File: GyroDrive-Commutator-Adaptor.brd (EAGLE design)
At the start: 108 x 76.2 mm, 26 parts, among them U1 HALL, U2 PCA9517, U3 5V, U4 2.5V, U5 INA2141U, U6 INA2141U, U7 INA2141U, X1 NORCOMP-DB25-SMD-MALE

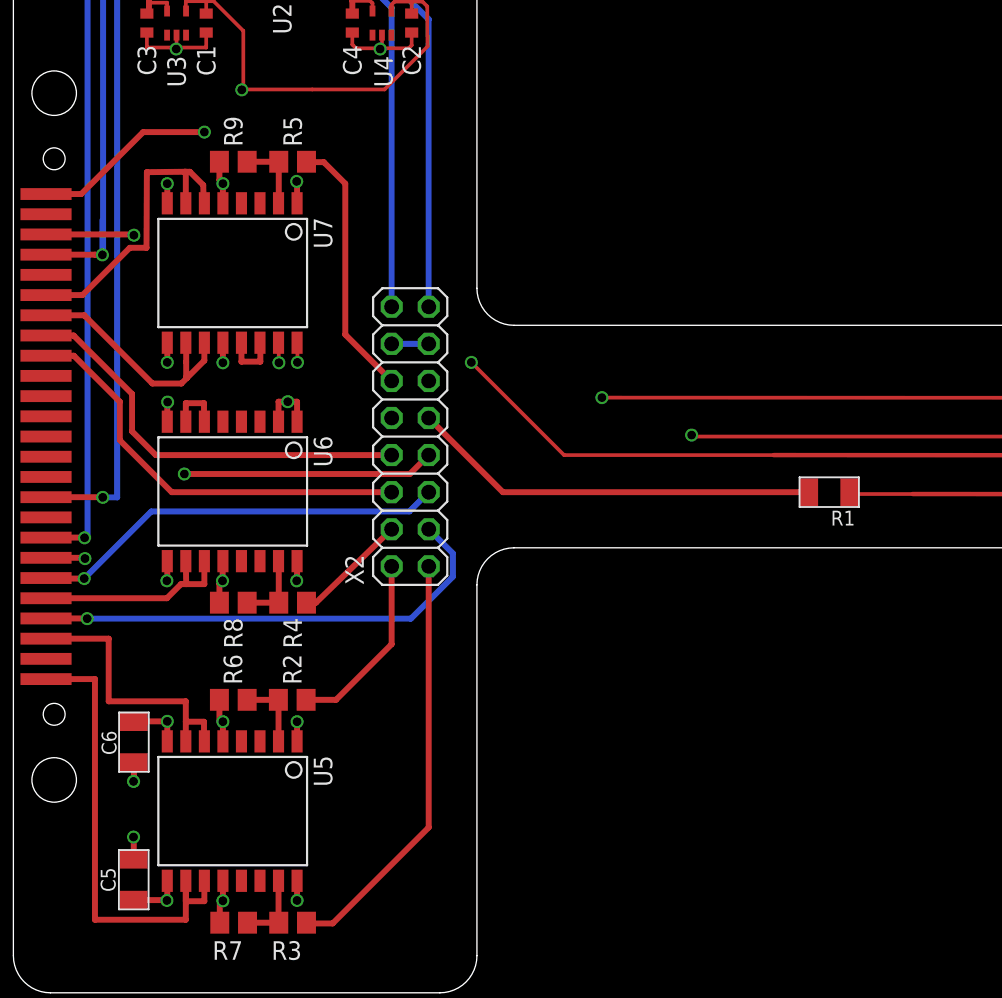
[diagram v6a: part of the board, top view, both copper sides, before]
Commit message: Fixed stop mask DRC errors on some resistors and capacitors
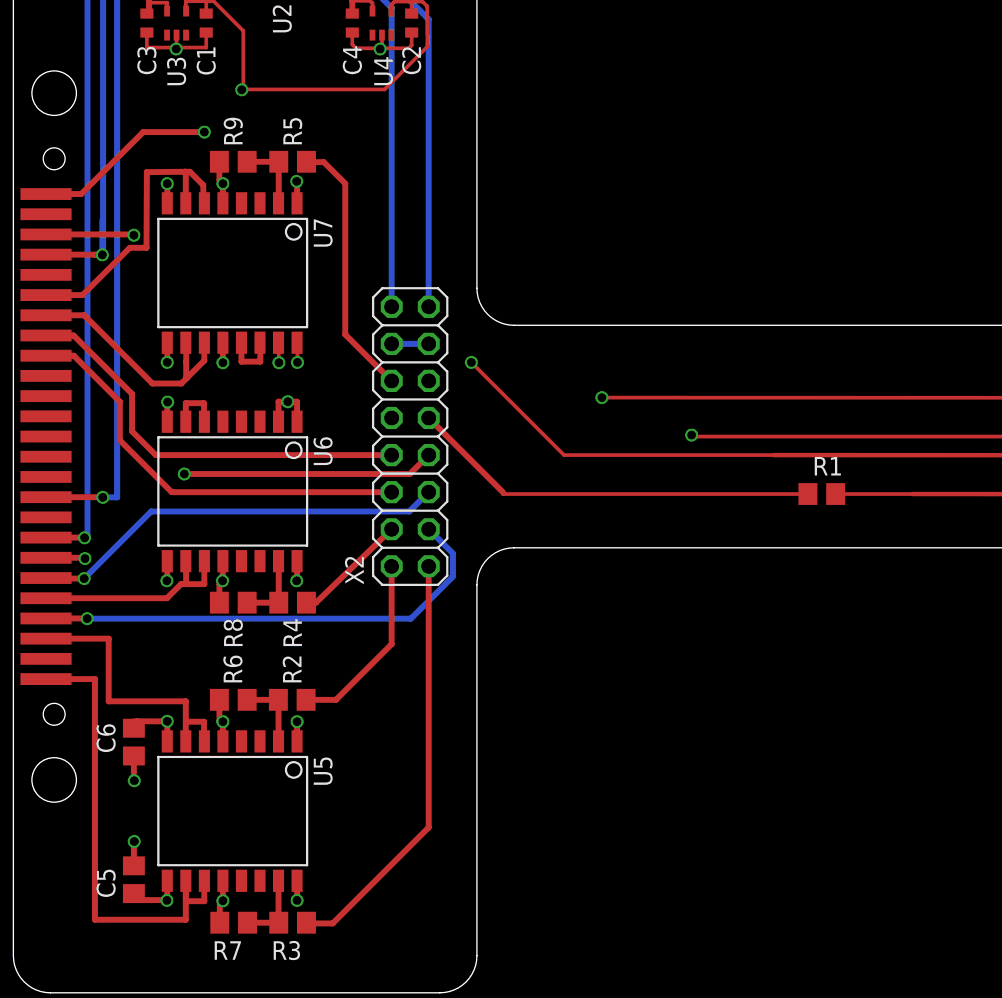
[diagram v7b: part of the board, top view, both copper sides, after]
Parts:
- C5, C6: device elm:R0805ELM -> resistor:C0805
- R1: device elm:R0805ELM -> resistor:R0805
- moved R1 0.52 mm to (55.4, 34.2), turned to 0 degrees
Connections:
- net V+: now also R1.1; no longer R1.2
- net V+_HALL: now also R1.2; no longer R1.1
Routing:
- net AGND: track 97.8 -> 99.9 mm
- net V-: track 73.9 -> 75.3 mm
- net V+_HALL: track 48.5 -> 49.4 mm
- net V+: track 185.1 -> 185.7 mm
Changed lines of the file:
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@@
 <attribute name="OC_FARNELL" value="1459468" x="-30.734" y="40.6908" size="1.778" layer="27" rot="R180" display="off"/>
-</element>
-<element name="R1" library="elm" package="R0805ELM" value="10k" x="55.88" y="34.29" rot="R180"/>
-<element name="C5" library="elm" package="R0805ELM" value="100nF" x="8.244471875" y="7.746809375" smashed="yes" rot="R90">
-<attribute name="NAME" x="6.999871875" y="7.746809375" size="1.016" layer="25" ratio="15" rot="R90" align="bottom-center"/>
-<attribute name="VALUE" x="8.244471875" y="7.772209375" size="1.016" layer="27" ratio="15" align="center"/>
-</element>
-<element name="C6" library="elm" package="R0805ELM" value="100nF" x="8.255" y="17.1704" smashed="yes" rot="R270">
-<attribute name="NAME" x="6.0452" y="17.9578" size="1.016" layer="25" ratio="15" rot="R270"/>
-<attribute name="VALUE" x="8.255" y="17.145" size="1.016" layer="27" ratio="15" rot="R180" align="center"/>
 </element>
 <element name="X2" library="pinhead" package="2X08" value="" x="27.178" y="38.1" rot="R90"/>
@@
 <attribute name="VALUE" x="10.7442" y="70.3072" size="1.27" layer="27" rot="R270"/>
 </element>
+<element name="R1" library="resistor" package="R0805" value="10k" x="55.372" y="34.163"/>
+<element name="C5" library="resistor" package="C0805" value="100nF" x="8.255" y="7.747" rot="R90"/>
+<element name="C6" library="resistor" package="C0805" value="100nF" x="8.255" y="17.1704" smashed="yes" rot="R270">
+<attribute name="NAME" x="5.715" y="18.4912" size="1.27" layer="25" rot="R270"/>
+<attribute name="VALUE" x="5.715" y="18.4404" size="1.27" layer="27" rot="R270"/>
+</element>
 </elements>
 <signals>
 <signal name="V-">
-<contactref element="C6" pad="1"/>
 <contactref element="U6" pad="8"/>
 <contactref element="U7" pad="8"/>
@@
 <wire x1="10.541" y1="18.5928" x2="10.5156" y2="18.542" width="0.4064" layer="2"/>
 <wire x1="10.5156" y1="18.542" x2="10.1346" y2="18.542" width="0.4064" layer="2"/>
-<wire x1="8.255" y1="18.5674" x2="8.255" y2="18.5928" width="0.4064" layer="1"/>
-<wire x1="8.255" y1="18.5928" x2="10.541" y2="18.5928" width="0.4064" layer="1"/>
+<wire x1="8.255" y1="18.5928" x2="8.4836" y2="18.5928" width="0.4064" layer="1"/>
+<wire x1="8.4836" y1="18.5928" x2="10.541" y2="18.5928" width="0.4064" layer="1"/>
 <wire x1="10.541" y1="39.116" x2="10.541" y2="40.4114" width="0.4064" layer="1"/>
 <wire x1="10.541" y1="40.4114" x2="10.5664" y2="40.4622" width="0.4064" layer="1"/>
@@
 <wire x1="11.7094" y1="35.5346" x2="9.45374375" y2="35.5346" width="0.4064" layer="2"/>
 <wire x1="9.45374375" y1="35.5346" x2="9.40294375" y2="35.4838" width="0.4064" layer="2"/>
+<contactref element="C6" pad="1"/>
+<wire x1="8.255" y1="18.1204" x2="8.1788" y2="18.1204" width="0.254" layer="1"/>
+<wire x1="8.1788" y1="18.1204" x2="8.1788" y2="17.8308" width="0.254" layer="1"/>
+<wire x1="8.1788" y1="17.8308" x2="8.4836" y2="17.8308" width="0.254" layer="1"/>
+<wire x1="8.4836" y1="17.8308" x2="8.4836" y2="18.5928" width="0.254" layer="1"/>
 </signal>
 <signal name="V+">
 <contactref element="U5" pad="9"/>
 <contactref element="U6" pad="9"/>
-<contactref element="R1" pad="2"/>
-<contactref element="C5" pad="1"/>
 <contactref element="U7" pad="9"/>
 <contactref element="X1" pad="P$1"/>
@@
 <via x="10.5156" y="6.3246" extent="1-16" drill="0.6"/>
 <wire x1="10.4902" y1="6.35" x2="10.5156" y2="6.3246" width="0.4064" layer="1"/>
-<wire x1="10.4902" y1="6.35" x2="8.2446625" y2="6.35" width="0.4064" layer="1"/>
-<wire x1="8.2446625" y1="6.35" x2="8.244471875" y2="6.349809375" width="0.4064" layer="1"/>
+<wire x1="10.4902" y1="6.35" x2="8.3566" y2="6.35" width="0.4064" layer="1"/>
 <via x="10.5156" y="28.2194" extent="1-16" drill="0.6"/>
+<wire x1="8.3566" y1="6.35" x2="8.2446625" y2="6.35" width="0.4064" layer="1"/>
 <wire x1="10.541" y1="44.5262" x2="10.541" y2="43.18" width="0.4064" layer="1"/>
 <via x="10.541" y="43.18" extent="1-16" drill="0.6"/>
@@
 <wire x1="15.6972" y1="61.8998" x2="15.6464" y2="61.849" width="0.4064" layer="2"/>
 <via x="15.6464" y="61.849" extent="1-16" drill="0.6"/>
-<wire x1="20.4724" y1="61.8744" x2="15.6718" y2="61.8744" width="0.254" layer="1"/>
 <wire x1="15.6718" y1="61.8744" x2="15.6464" y2="61.849" width="0.4064" layer="1"/>
 <wire x1="12.3698" y1="58.9534" x2="13.081" y2="58.9534" width="0.4064" layer="2"/>
-<wire x1="54.483" y1="34.29" x2="33.528" y2="34.29" width="0.4064" layer="1"/>
 <wire x1="33.528" y1="34.29" x2="28.448" y2="39.37" width="0.4064" layer="1"/>
 <wire x1="28.448" y1="39.37" x2="27.2034" y2="38.1254" width="0.4064" layer="2"/>
@@
 <wire x1="26.1112" y1="67.8942" x2="27.2796" y2="67.8942" width="0.254" layer="1"/>
 <wire x1="27.2796" y1="67.8942" x2="27.2796" y2="67.071" width="0.254" layer="1"/>
-<wire x1="20.4724" y1="61.8744" x2="25.4254" y2="61.8744" width="0.254" layer="1"/>
+<wire x1="15.6718" y1="61.8744" x2="25.4254" y2="61.8744" width="0.254" layer="1"/>
 <wire x1="25.4254" y1="61.8744" x2="28.3718" y2="64.8208" width="0.254" layer="1"/>
 <wire x1="28.3718" y1="64.8208" x2="28.3464" y2="67.564" width="0.254" layer="1"/>
 <wire x1="27.2796" y1="67.8942" x2="28.0162" y2="67.8942" width="0.254" layer="1"/>
 <wire x1="28.0162" y1="67.8942" x2="28.3464" y2="67.564" width="0.254" layer="1"/>
+<contactref element="R1" pad="1"/>
+<wire x1="54.422" y1="34.163" x2="33.528" y2="34.163" width="0.254" layer="1"/>
+<wire x1="33.528" y1="34.163" x2="33.528" y2="34.29" width="0.254" layer="1"/>
+<contactref element="C5" pad="1"/>
+<wire x1="8.255" y1="6.797" x2="8.3566" y2="6.797" width="0.254" layer="1"/>
+<wire x1="8.3566" y1="6.797" x2="8.3566" y2="6.35" width="0.254" layer="1"/>
 </signal>
 <signal name="HALL0">
@@
 </signal>
 <signal name="V+_HALL">
-<contactref element="R1" pad="1"/>
 <contactref element="U1" pad="C"/>
 <wire x1="61.595" y1="34.163" x2="103.0732" y2="34.1376" width="0.3048" layer="1"/>
@@
 <wire x1="104.4702" y1="35.5346" x2="104.8512" y2="35.5346" width="0.3048" layer="1"/>
 <wire x1="104.8512" y1="35.5346" x2="104.5464" y2="35.5854" width="0.3048" layer="1"/>
-<wire x1="61.595" y1="34.163" x2="57.404" y2="34.163" width="0.254" layer="1"/>
-<wire x1="57.404" y1="34.163" x2="57.277" y2="34.29" width="0.254" layer="1"/>
+<wire x1="61.595" y1="34.163" x2="56.322" y2="34.163" width="0.254" layer="1"/>
+<contactref element="R1" pad="2"/>
 </signal>
 <signal name="E3">
@@
 <contactref element="U5" pad="12"/>
 <contactref element="U6" pad="12"/>
-<contactref element="C5" pad="2"/>
-<contactref element="C6" pad="2"/>
 <contactref element="U1" pad="A"/>
 <contactref element="U7" pad="5"/>
@@
 <via x="14.351" y="18.5674" extent="1-16" drill="0.6"/>
 <wire x1="14.351" y1="18.5674" x2="14.478" y2="19.0246" width="0.4064" layer="15"/>
-<via x="8.2296" y="10.668" extent="1-16" drill="0.6"/>
 <wire x1="14.351" y1="7.6708" x2="14.351" y2="6.2992" width="0.4064" layer="1"/>
 <via x="14.351" y="6.2992" extent="1-16" drill="0.6"/>
 <wire x1="14.351" y1="6.2992" x2="14.351" y2="5.5372" width="0.4064" layer="15"/>
 <wire x1="14.351" y1="5.5372" x2="14.3256" y2="5.5372" width="0.4064" layer="15"/>
-<wire x1="8.244471875" y1="9.143809375" x2="8.244471875" y2="10.668" width="0.4064" layer="1"/>
-<wire x1="8.244471875" y1="10.668" x2="8.2296" y2="10.668" width="0.4064" layer="1"/>
-<wire x1="8.255" y1="15.7734" x2="8.255" y2="14.5542" width="0.4064" layer="1"/>
-<wire x1="8.255" y1="14.5542" x2="8.2296" y2="14.478" width="0.4064" layer="1"/>
-<via x="8.2296" y="14.478" extent="1-16" drill="0.6"/>
-<wire x1="8.2296" y1="14.478" x2="8.3058" y2="14.5034" width="0.4064" layer="15"/>
-<wire x1="8.3058" y1="14.5034" x2="8.7884" y2="14.5034" width="0.4064" layer="15"/>
 <wire x1="14.351" y1="29.5656" x2="14.3256" y2="28.2194" width="0.4064" layer="1"/>
 <via x="14.3256" y="28.2194" extent="1-16" drill="0.6"/>
@@
 <wire x1="46.5582" y1="38.1" x2="46.4566" y2="38.2016" width="0.4064" layer="1"/>
 <via x="46.4566" y="38.2016" extent="1-16" drill="0.6"/>
+<contactref element="C5" pad="2"/>
+<contactref element="C6" pad="2"/>
+<wire x1="8.255" y1="16.2204" x2="8.255" y2="14.5288" width="0.4064" layer="1"/>
+<wire x1="8.255" y1="14.5288" x2="8.2804" y2="14.5288" width="0.4064" layer="1"/>
+<via x="8.2804" y="14.5288" extent="1-16" drill="0.6"/>
+<wire x1="8.2804" y1="14.5288" x2="8.2804" y2="13.716" width="0.4064" layer="15"/>
+<wire x1="8.2804" y1="13.716" x2="8.4582" y2="13.716" width="0.4064" layer="15"/>
+<wire x1="8.255" y1="8.697" x2="8.255" y2="10.3632" width="0.4064" layer="1"/>
+<wire x1="8.255" y1="10.3632" x2="8.2804" y2="10.3632" width="0.4064" layer="1"/>
+<via x="8.2804" y="10.3632" extent="1-16" drill="0.6"/>
+<wire x1="8.2804" y1="10.3632" x2="8.2804" y2="10.795" width="0.4064" layer="15"/>
+<wire x1="8.2804" y1="10.795" x2="8.9916" y2="10.795" width="0.4064" layer="15"/>
 </signal>
 <signal name="MOTORGND">

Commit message: no message
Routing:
- net ICOM: track 29.1 -> 29.2 mm, vias 0 -> 1
- net IX: vias 0 -> 1
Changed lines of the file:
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@@
 <contactref element="X2" pad="8"/>
 <wire x1="2.2352" y1="45.0215" x2="4.1275" y2="45.0215" width="0.4064" layer="1"/>
-<wire x1="25.908" y1="36.83" x2="9.7536" y2="36.83" width="0.4064" layer="1"/>
-<wire x1="9.7536" y1="36.83" x2="8.128" y2="38.4556" width="0.4064" layer="1"/>
-<wire x1="8.128" y1="38.4556" x2="8.128" y2="41.021" width="0.4064" layer="1"/>
+<wire x1="25.908" y1="36.83" x2="9.7536" y2="36.83" width="0.4064" layer="16"/>
+<wire x1="9.7536" y1="36.83" x2="8.128" y2="38.4556" width="0.4064" layer="16"/>
+<wire x1="8.128" y1="38.4556" x2="8.128" y2="41.021" width="0.4064" layer="16"/>
 <wire x1="8.128" y1="41.021" x2="4.1275" y2="45.0215" width="0.4064" layer="1"/>
+<via x="8.128" y="41.021" extent="1-16" drill="0.6"/>
 </signal>
 <signal name="ICOM">
@@
 <wire x1="2.2352" y1="43.6372" x2="4.1402" y2="43.6372" width="0.4064" layer="1"/>
 <wire x1="4.1402" y1="43.6372" x2="7.2898" y2="40.4876" width="0.4064" layer="1"/>
-<wire x1="7.2898" y1="40.4876" x2="7.2898" y2="37.846" width="0.4064" layer="1"/>
-<wire x1="7.2898" y1="37.846" x2="10.8458" y2="34.29" width="0.4064" layer="1"/>
-<wire x1="10.8458" y1="34.29" x2="25.908" y2="34.29" width="0.4064" layer="1"/>
+<wire x1="7.2898" y1="40.4876" x2="7.2898" y2="37.5158" width="0.4064" layer="1"/>
+<wire x1="7.2898" y1="37.5158" x2="8.3312" y2="36.4744" width="0.4064" layer="1"/>
+<wire x1="8.3312" y1="36.4744" x2="10.8458" y2="34.29" width="0.4064" layer="16"/>
+<wire x1="10.8458" y1="34.29" x2="25.908" y2="34.29" width="0.4064" layer="16"/>
+<via x="8.3312" y="36.4744" extent="1-16" drill="0.6"/>
 </signal>
 <signal name="E4">
